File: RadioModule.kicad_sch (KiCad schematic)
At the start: 4 parts, among them U1 SX1280IMLTRT

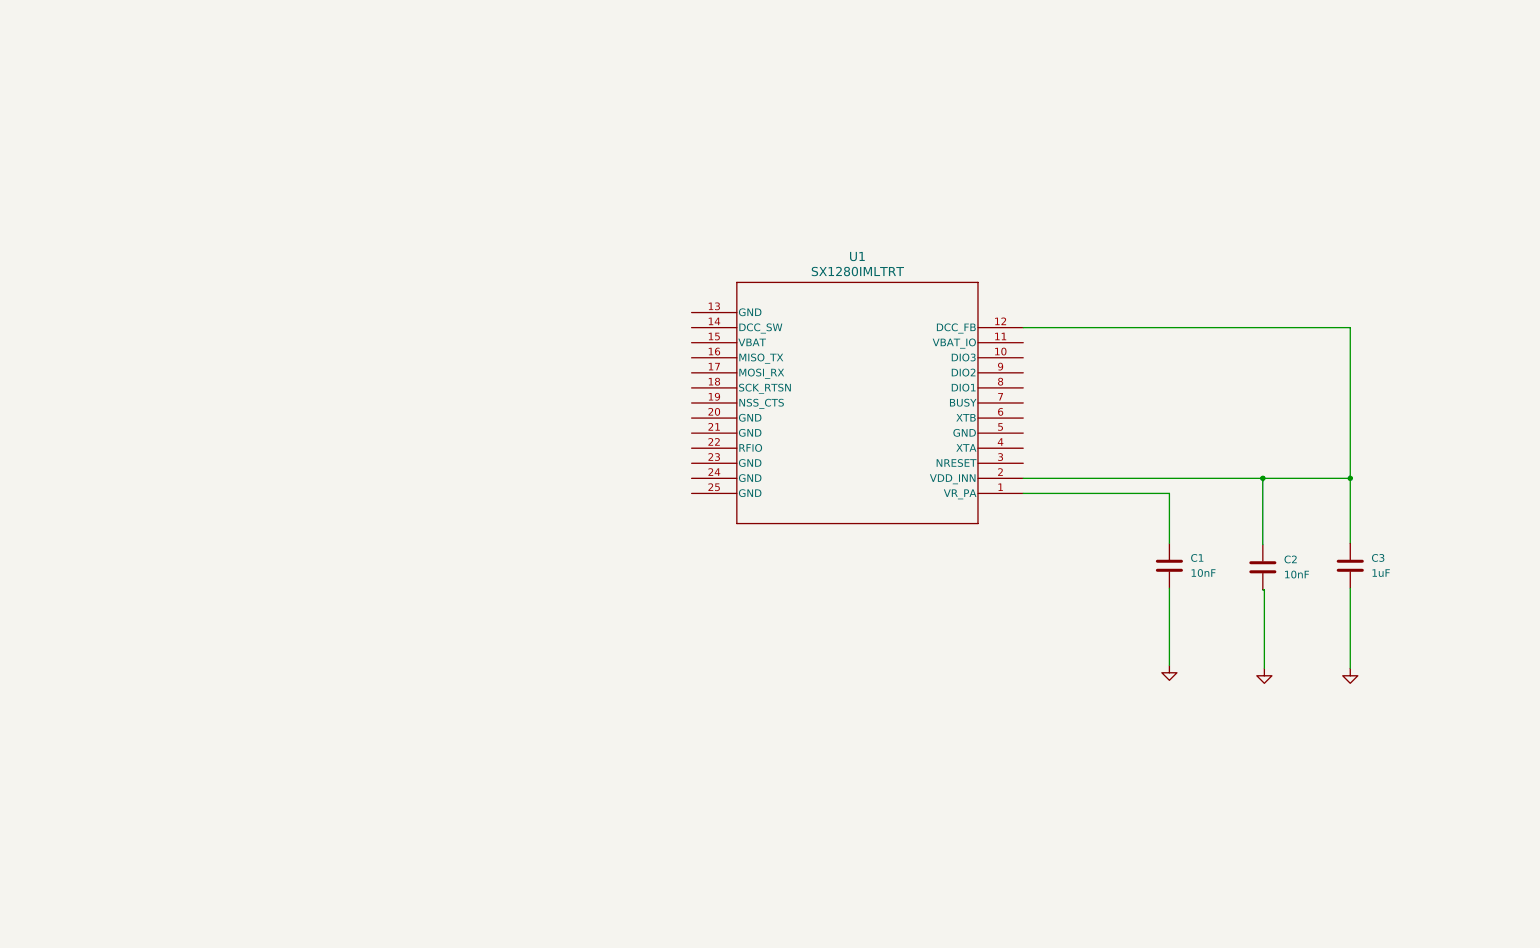
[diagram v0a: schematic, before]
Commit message: Finished Radio Module Schematic
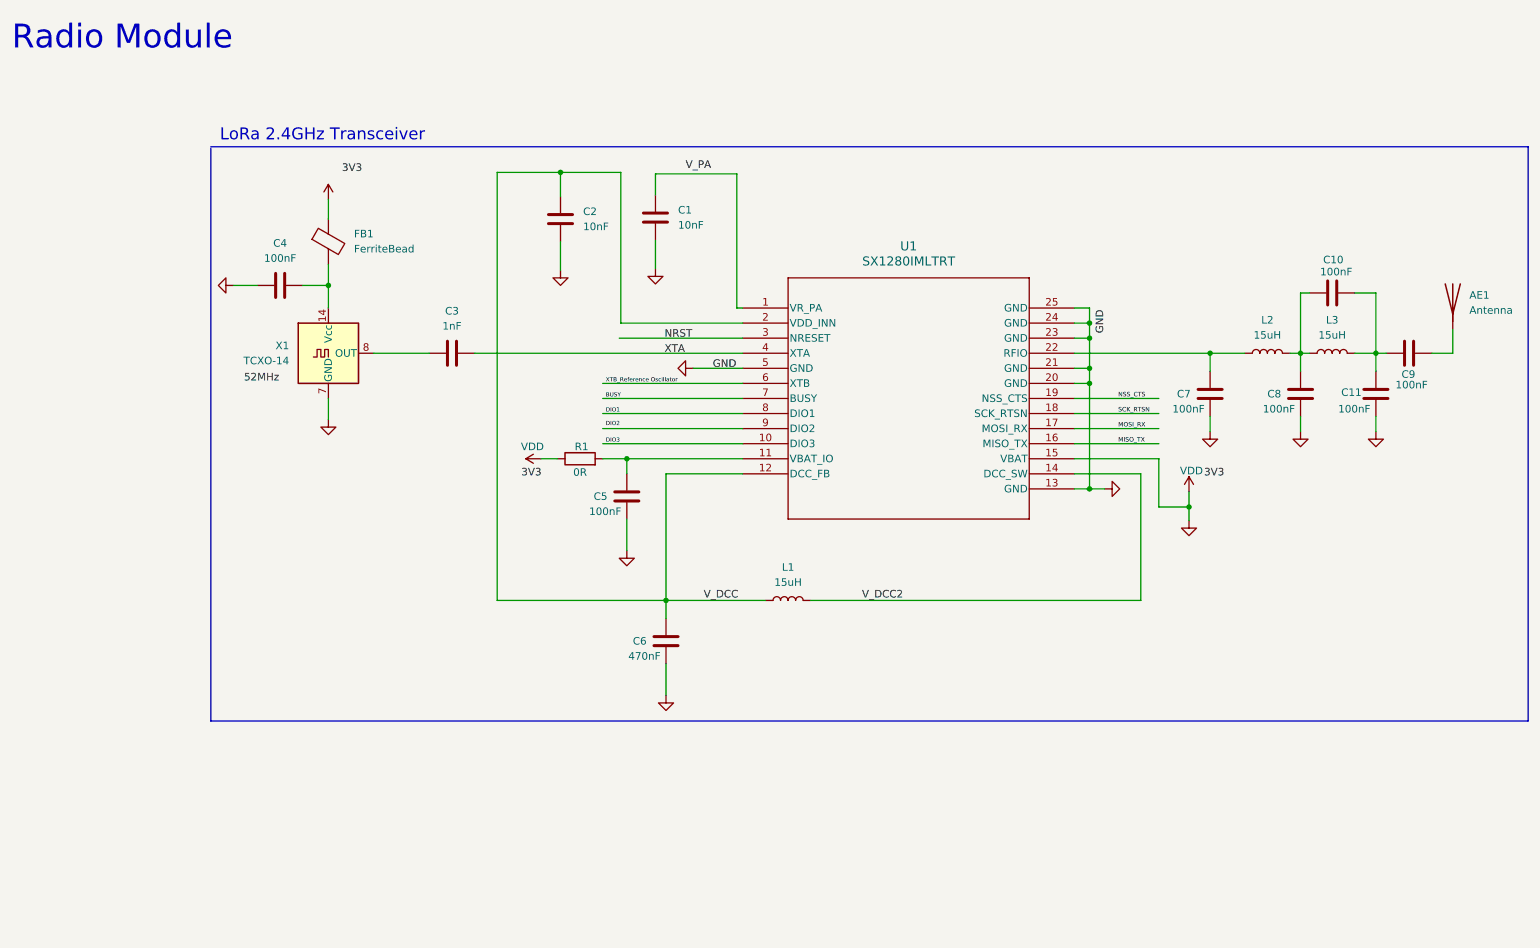
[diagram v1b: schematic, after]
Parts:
- added AE1: Antenna, symbol Device:Antenna
- added C10, C11, C4, C5, C7, C8, C9: 100nF, symbol Device:C
- added C6: 470nF, symbol Device:C
- added FB1: FerriteBead, symbol Device:FerriteBead
- added L1, L2, L3: 15uH, symbol Device:L
- added R1: 0R, symbol Device:R
- added X1: TCXO-14, Oscillator:Oscillator_DIP-14, symbol Oscillator:TCXO-14
- C3: value 1uF -> 1nF
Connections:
- net GND: now also U1.13 (GND), U1.15 (VBAT), U1.20 (GND), U1.21 (GND), U1.23 (GND), U1.24 (GND), U1.25 (GND), U1.5 (GND), C11.2, C4.2, C5.2, C6.2, C7.2, C8.2, FB1.1, R1.1, X1.7 (GND); no longer C3.2
- net V_DCC: now reaches C2.1, U1.12 (DCC_FB), U1.2 (VDD_INN)
- net V_DCC: now also C6.1, L1.1; no longer C3.1
- net DIO3: now reaches U1.10 (DIO3)
- net at U1.11 (VBAT_IO): now also C5.1, R1.2
- net V_DCC2: now reaches U1.14 (DCC_SW)
- net V_DCC2: now also L1.2
- net MISO_TX: now reaches U1.16 (MISO_TX)
- net MOSI_RX: now reaches U1.17 (MOSI_RX)
- net SCK_RTSN: now reaches U1.18 (SCK_RTSN)
- net NSS_CTS: now reaches U1.19 (NSS_CTS)
- net at U1.22 (RFIO): now also C7.1, L2.1
- net at U1.4 (XTA): now also C3.1
- net XTB_Reference Oscillator: now reaches U1.6 (XTB)
- net BUSY: now reaches U1.7 (BUSY)
- net DIO1: now reaches U1.8 (DIO1)
- new net: C10.2, C8.1, L2.2, L3.1
- new net: C4.1, FB1.2, X1.14 (Vcc)
- new net: C10.1, C11.1, C9.2, L3.2
- new net: C3.2, X1.8 (OUT)
- new net: AE1.1 (A), C9.1
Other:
- note added: "LoRa 2.4GHz Transceiver"
- note added: "Radio Module"
- moved on the sheet: U1

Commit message: Radio Schematic Update 1
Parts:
- removed FB1: FerriteBead, symbol Device:FerriteBead
- removed X1: TCXO-14, Oscillator:Oscillator_DIP-14, symbol Oscillator:TCXO-14
- added Y1: ABM13W-52.0MHz, symbol Device:Crystal_GND24
- C4: value 100nF -> 1nF
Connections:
- net DIO2: now also U1.9 (DIO2)
- net GND: now also C3.1, C4.1, Y1.2, Y1.4; no longer C4.2
- net NRST: now also U1.3 (NRESET)
- net V_PA: now also C1.1, U1.1 (VR_PA)
- net XTA: now also C4.2, U1.4 (XTA), Y1.3
- net XTB_Reference Oscillator: now also C3.2, Y1.1

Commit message: Radio Module Update 2
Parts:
- removed AE1: Antenna, symbol Device:Antenna
- added J1, J10, J11, J12, J13, J14, J15, J16, J2, J3, J4, J5, J6, J7, J8, J9: Conn_01x01_Pin, Connector_Wire:SolderWirePad_1x01_SMD_1x2mm, symbol Connector:Conn_01x01_Pin
- C1, C10, C11, C2, C3, C4, C5, C7, C8, C9: footprint (none) -> Capacitor_SMD:C_0402_1005Metric
- C6: footprint (none) -> Capacitor_SMD:C_0603_1608Metric
- L1, L2, L3: footprint (none) -> Inductor_SMD:L_0402_1005Metric
- R1: footprint (none) -> Resistor_SMD:R_0402_1005Metric
- Y1: footprint (none) -> Crystal:Crystal_SMD_2016-4Pin_2.0x1.6mm
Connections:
- net GND: now also J16.1 (Pin_1), J2.1 (Pin_1), J9.1 (Pin_1); no longer R1.1, U1.15 (VBAT)
- net NRST: now also J11.1 (Pin_1)
- net ANT: now reaches C9.1
- net ANT: now also J1.1 (Pin_1)
- net BUSY: no longer names the net of U1.7 (BUSY)
- net DIO1 renamed INT
- net INT: now also J6.1 (Pin_1)
- net DIO2: no longer names the net of U1.9 (DIO2)
- net DIO3: no longer names the net of U1.10 (DIO3)
- net MISO_TX renamed MISO
- net MISO: now also J15.1 (Pin_1)
- net MOSI_RX renamed MOSI
- net MOSI: now also J14.1 (Pin_1)
- net NSS_CTS renamed CS
- net CS: now also J12.1 (Pin_1)
- net SCK_RTSN renamed SCK
- net SCK: now also J13.1 (Pin_1)
- new net 3V3: J5.1 (Pin_1), R1.1, U1.15 (VBAT)
- no-connect marks 0 -> 8
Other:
- note added: "Castellated Pin Connections"

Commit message: Post Board Review Update
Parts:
- removed C10, C8, C9: 100nF, Capacitor_SMD:C_0402_1005Metric, symbol Device:C
- added C12, C13, C14: 100nF, Capacitor_SMD:C_0402_1005Metric, symbol Device:C
- L1: footprint Inductor_SMD:L_0402_1005Metric -> Inductor_SMD:L_0805_2012Metric
- U1: footprint QFN24_4X4_SEM -> SX1280IMLTRT:QFN24_4X4_SEM
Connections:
- net ANT: now also C14.1
- net GND: now also C13.2
- net at L2.2, L3.1: now also C11.1, C12.2
- net DIO3: now reaches U1.10 (DIO3)
- net DIO3: now also J3.1 (Pin_1)
- net DIO2: now reaches U1.9 (DIO2)
- net DIO2: now also J8.1 (Pin_1)
- net at L3.2: now also C12.1, C13.1, C14.2; no longer C11.1
- net DIO4: now reaches J4.1 (Pin_1)
- net DIO5: now reaches J10.1 (Pin_1)
- net DIO1: now reaches J7.1 (Pin_1)
- no-connect marks 8 -> 1

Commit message: lets try that again
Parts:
- added C8: 100nF, Capacitor_SMD:C_0402_1005Metric, symbol Device:C
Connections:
- net 3V3: now also C8.1
- net GND: now also C8.2
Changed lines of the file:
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@@
   (junction (at 204.47 76.962) (diameter 0) (color 0 0 0 0)
+  )
+  (junction (at 208.788 89.662) (diameter 0) (color 0 0 0 0)
   )
   (junction (at 109.728 41.402) (diameter 0) (color 0 0 0 0)
@@
     (stroke (width 0) (type default))
   )
+  (wire (pts (xy 208.788 82.042) (xy 208.788 79.502))
+    (stroke (width 0) (type default))
+  )
   (wire (pts (xy 196.342 69.342) (xy 204.47 69.342))
     (stroke (width 0) (type default))
@@
     (stroke (width 0) (type default))
   )
-  (wire (pts (xy 196.342 89.662) (xy 210.566 89.662))
+  (wire (pts (xy 196.342 89.662) (xy 208.788 89.662))
     (stroke (width 0) (type default))
   )
@@
   )
   (wire (pts (xy 125.73 41.656) (xy 125.73 45.212))
+    (stroke (width 0) (type default))
+  )
+  (wire (pts (xy 208.788 89.662) (xy 210.566 89.662))
     (stroke (width 0) (type default))
   )
@@
         (path "/0d0e4888-cfb8-427f-88cf-46e56f13629b"
           (reference "C4") (unit 1)
+        )
+      )
+    )
+  )
+  (symbol (lib_id "Device:C") (at 208.788 85.852 180) (unit 1)
+    (in_bom yes) (on_board yes) (dnp no)
+    (property "Reference" "C8" (at 214.376 85.852 0)
+      (effects (font (size 1.27 1.27)) (justify left))
+    )
+    (property "Value" "100nF" (at 215.138 83.312 0)
+      (effects (font (size 1.27 1.27)) (justify left))
+    )
+    (property "Footprint" "Capacitor_SMD:C_0402_1005Metric" (at 207.8228 82.042 0)
+      (effects (font (size 1.27 1.27)) hide)
+    )
+    (property "Datasheet" "~" (at 208.788 85.852 0)
+      (effects (font (size 1.27 1.27)) hide)
+    )
+    (pin "1")
+    (pin "2")
+    (instances
+      (project "RadioModule"
+        (path "/0d0e4888-cfb8-427f-88cf-46e56f13629b"
+          (reference "C8") (unit 1)
+        )
+      )
+      (project "Radio Board"
+        (path "/96645608-7ae7-41a0-a771-05df995caccb/85d7d8f7-7be3-46a3-a33d-de1e25797b47"
+          (reference "C20") (unit 1)
+        )
+      )
+      (project "Radio Module"
+        (path "/e0aafefc-63ce-4fcc-91f2-fb3da4e79e9e"
+          (reference "C7") (unit 1)
         )
       )
@@
         )
       )
+    )
+  )
+  (symbol (lib_id "power:GND") (at 208.788 79.502 180) (unit 1)
+    (in_bom yes) (on_board yes) (dnp no) (fields_autoplaced)
+    (property "Reference" "#PWR012" (at 208.788 73.152 0)
+      (effects (font (size 1.27 1.27)) hide)
+    )
+    (property "Value" "GND" (at 208.788 74.93 0)
+      (effects (font (size 1.27 1.27)) hide)
+    )
+    (property "Footprint" "" (at 208.788 79.502 0)
+      (effects (font (size 1.27 1.27)) hide)
+    )
+    (property "Datasheet" "" (at 208.788 79.502 0)
+      (effects (font (size 1.27 1.27)) hide)
+    )
+    (pin "1")
+    (instances
+      (project "RadioModule"
+        (path "/0d0e4888-cfb8-427f-88cf-46e56f13629b"
+          (reference "#PWR012") (unit 1)
+        )
+      )

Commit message: made it less clapped
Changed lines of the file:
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@@
+    (stroke (width 0) (type default))
+  )
+  (wire (pts (xy 211.836 77.47) (xy 211.836 78.74))
     (stroke (width 0) (type default))
   )
@@
     (stroke (width 0) (type default))
   )
-  (wire (pts (xy 208.788 82.042) (xy 208.788 79.502))
+  (wire (pts (xy 91.694 60.96) (xy 97.028 60.96))
+    (stroke (width 0) (type default))
+  )
+  (wire (pts (xy 208.788 77.47) (xy 211.836 77.47))
     (stroke (width 0) (type default))
   )
@@
     (stroke (width 0) (type default))
   )
-  (wire (pts (xy 91.694 57.912) (xy 91.694 60.96))
-    (stroke (width 0) (type default))
-  )
   (wire (pts (xy 127.508 113.538) (xy 127.508 116.586))
     (stroke (width 0) (type default))
@@
   )
   (wire (pts (xy 196.342 92.202) (xy 207.518 92.202))
+    (stroke (width 0) (type default))
+  )
+  (wire (pts (xy 208.788 82.042) (xy 208.788 77.47))
     (stroke (width 0) (type default))
   )
@@
     )
   )
-  (symbol (lib_id "power:GND") (at 208.788 79.502 180) (unit 1)
-    (in_bom yes) (on_board yes) (dnp no) (fields_autoplaced)
-    (property "Reference" "#PWR012" (at 208.788 73.152 0)
-      (effects (font (size 1.27 1.27)) hide)
-    )
-    (property "Value" "GND" (at 208.788 74.93 0)
-      (effects (font (size 1.27 1.27)) hide)
-    )
-    (property "Footprint" "" (at 208.788 79.502 0)
-      (effects (font (size 1.27 1.27)) hide)
-    )
-    (property "Datasheet" "" (at 208.788 79.502 0)
+  (symbol (lib_id "power:GND") (at 211.836 78.74 0) (unit 1)
+    (in_bom yes) (on_board yes) (dnp no) (fields_autoplaced)
+    (property "Reference" "#PWR012" (at 211.836 85.09 0)
+      (effects (font (size 1.27 1.27)) hide)
+    )
+    (property "Value" "GND" (at 211.836 83.312 0)
+      (effects (font (size 1.27 1.27)) hide)
+    )
+    (property "Footprint" "" (at 211.836 78.74 0)
+      (effects (font (size 1.27 1.27)) hide)
+    )
+    (property "Datasheet" "" (at 211.836 78.74 0)
       (effects (font (size 1.27 1.27)) hide)
     )
@@
     )
   )
-  (symbol (lib_id "power:GND") (at 91.694 57.912 180) (unit 1)
-    (in_bom yes) (on_board yes) (dnp no) (fields_autoplaced)
-    (property "Reference" "#PWR04" (at 91.694 51.562 0)
-      (effects (font (size 1.27 1.27)) hide)
-    )
-    (property "Value" "GND" (at 91.694 53.34 0)
-      (effects (font (size 1.27 1.27)) hide)
-    )
-    (property "Footprint" "" (at 91.694 57.912 0)
-      (effects (font (size 1.27 1.27)) hide)
-    )
-    (property "Datasheet" "" (at 91.694 57.912 0)
-      (effects (font (size 1.27 1.27)) hide)
-    )
+  (symbol (lib_id "power:GND") (at 97.028 60.96 0) (unit 1)
+    (in_bom yes) (on_board yes) (dnp no) (fields_autoplaced)
+    (property "Reference" "#PWR04" (at 97.028 67.31 0)
+      (effects (font (size 1.27 1.27)) hide)
+    )
+    (property "Value" "GND" (at 97.028 65.532 0)
+      (effects (font (size 1.27 1.27)) hide)
+    )
+    (property "Footprint" "" (at 97.028 60.96 0)
+      (effects (font (size 1.27 1.27)) hide)
+    )
+    (property "Datasheet" "" (at 97.028 60.96 0)
+      (effects (font (size 1.27 1.27)) hide)
+    )

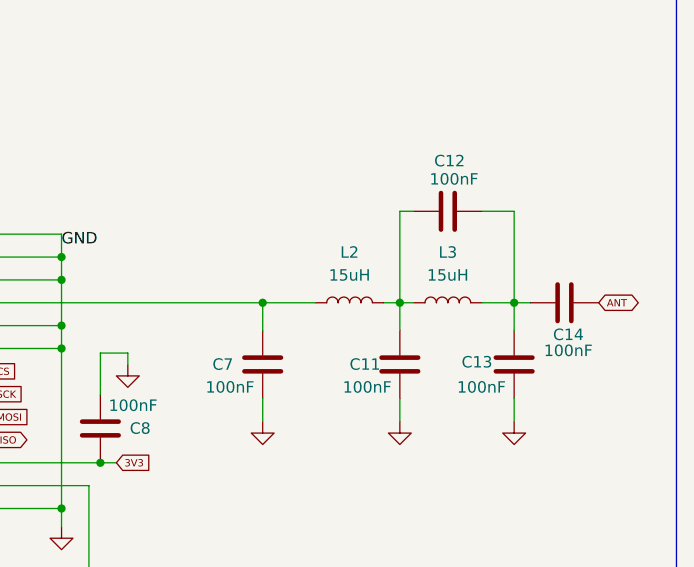
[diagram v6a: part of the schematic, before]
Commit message: Added silkscreen and changed pi filter component values
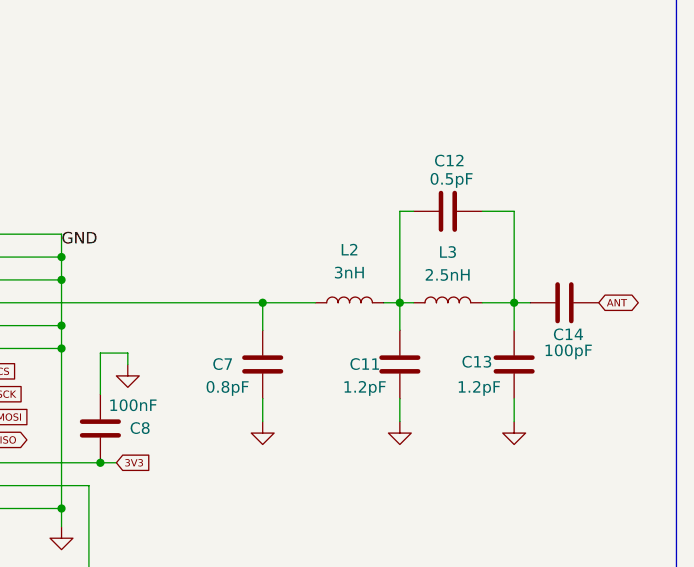
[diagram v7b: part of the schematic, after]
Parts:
- C11, C13: value 100nF -> 1.2pF
- C12: value 100nF -> 0.5pF
- C14: value 100nF -> 100pF
- C7: value 100nF -> 0.8pF
- L2: value 15uH -> 3nH
- L3: value 15uH -> 2.5nH
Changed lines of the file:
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@@
       (effects (font (size 1.27 1.27)) (justify left))
     )
-    (property "Value" "100nF" (at 220.472 81.28 0)
+    (property "Value" "0.8pF" (at 220.472 81.28 0)
       (effects (font (size 1.27 1.27)) (justify left))
     )
@@
   (symbol (lib_id "Device:L") (at 236.474 71.882 90) (unit 1)
     (in_bom yes) (on_board yes) (dnp no) (fields_autoplaced)
-    (property "Reference" "L2" (at 236.474 66.294 90)
-      (effects (font (size 1.27 1.27)))
-    )
-    (property "Value" "15uH" (at 236.474 68.834 90)
+    (property "Reference" "L2" (at 236.474 66.04 90)
+      (effects (font (size 1.27 1.27)))
+    )
+    (property "Value" "3nH" (at 236.474 68.58 90)
       (effects (font (size 1.27 1.27)))
     )
@@
       (effects (font (size 1.27 1.27)) (justify left))
     )
-    (property "Value" "100nF" (at 258.064 77.216 90)
+    (property "Value" "100pF" (at 258.064 77.216 90)
       (effects (font (size 1.27 1.27)) (justify left))
     )
@@
       (effects (font (size 1.27 1.27)))
     )
-    (property "Value" "15uH" (at 247.396 68.834 90)
+    (property "Value" "2.5nH" (at 247.396 68.834 90)
       (effects (font (size 1.27 1.27)))
     )
@@
       (effects (font (size 1.27 1.27)) (justify left))
     )
-    (property "Value" "100nF" (at 248.412 81.28 0)
+    (property "Value" "1.2pF" (at 248.412 81.28 0)
       (effects (font (size 1.27 1.27)) (justify left))
     )
@@
       (effects (font (size 1.27 1.27)) (justify left))
     )
-    (property "Value" "100nF" (at 245.364 58.166 90)
+    (property "Value" "0.5pF" (at 245.364 58.166 90)
       (effects (font (size 1.27 1.27)) (justify left))
     )
@@
       (effects (font (size 1.27 1.27)) (justify left))
     )
-    (property "Value" "100nF" (at 235.712 81.28 0)
-      (effects (font (size 1.27 1.27)) (justify left))
-    )
+    (property "Value" "1.2pF" (at 235.712 81.28 0)
+      (effects (font (size 1.27 1.27)) (justify left))
+    )
